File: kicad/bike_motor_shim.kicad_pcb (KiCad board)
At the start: 2 copper layers, 26.7 x 19 mm, 13 parts, among them J1 Conn_01x06_Male, J2 Conn_01x06_Male, K1 MSxx-1Axx-75, U1 ATtiny45-20SU, U2 MCP1700-5002E_SOT23, Y1 Crystal_Small

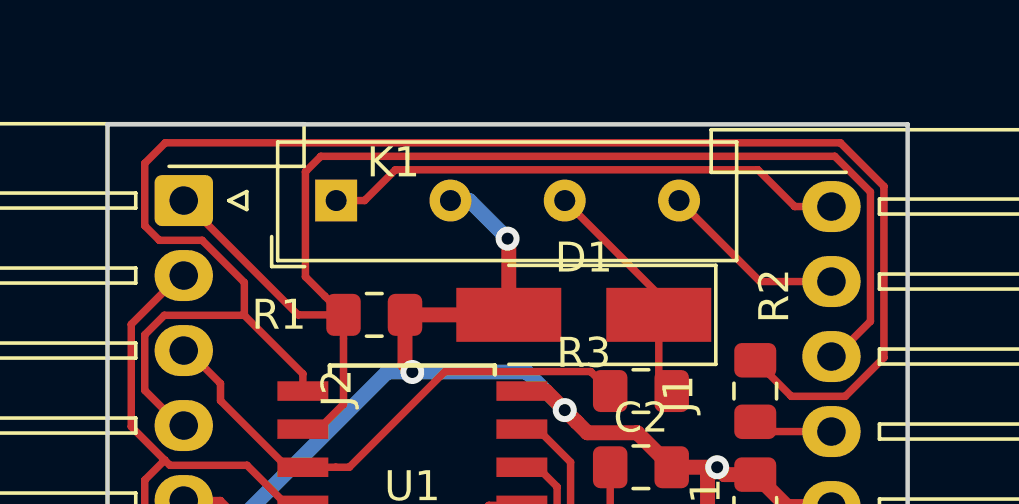
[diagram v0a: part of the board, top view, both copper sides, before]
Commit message: Fixed relay footprint
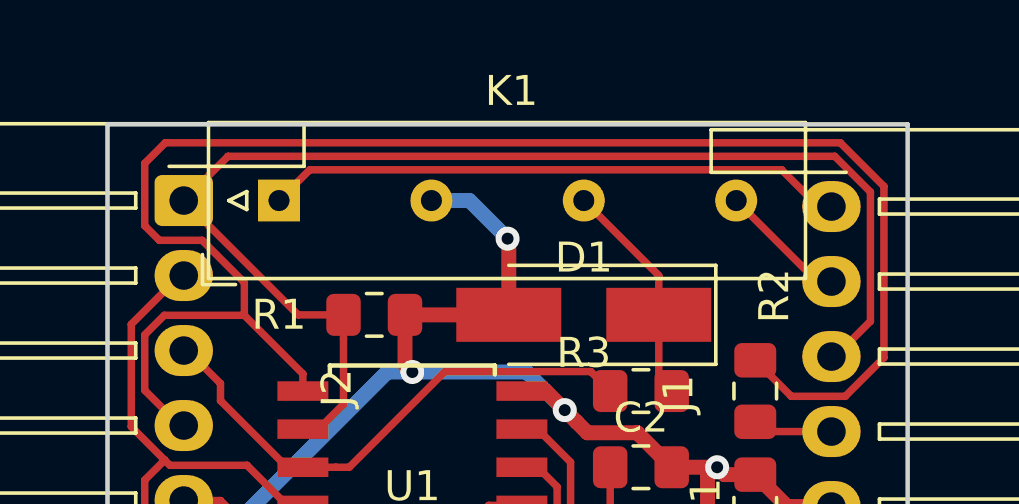
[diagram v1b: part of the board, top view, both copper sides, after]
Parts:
- K1: footprint Relay_THT:Relay_SPST_StandexMeder_MS_Form1AB -> Relay_THT:Relay_SPST_StandexMeder_SIL_Form1A
- moved K1 1.91 mm to (142.9, 112.4)
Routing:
- net MOTOR_OUT: track 6.20 -> 4.29 mm
- net MOTOR_IN: track 17.4 -> 19.3 mm
- net MISO: track 42.5 -> 41.7 mm
- net GND: track 40.7 -> 41.3 mm

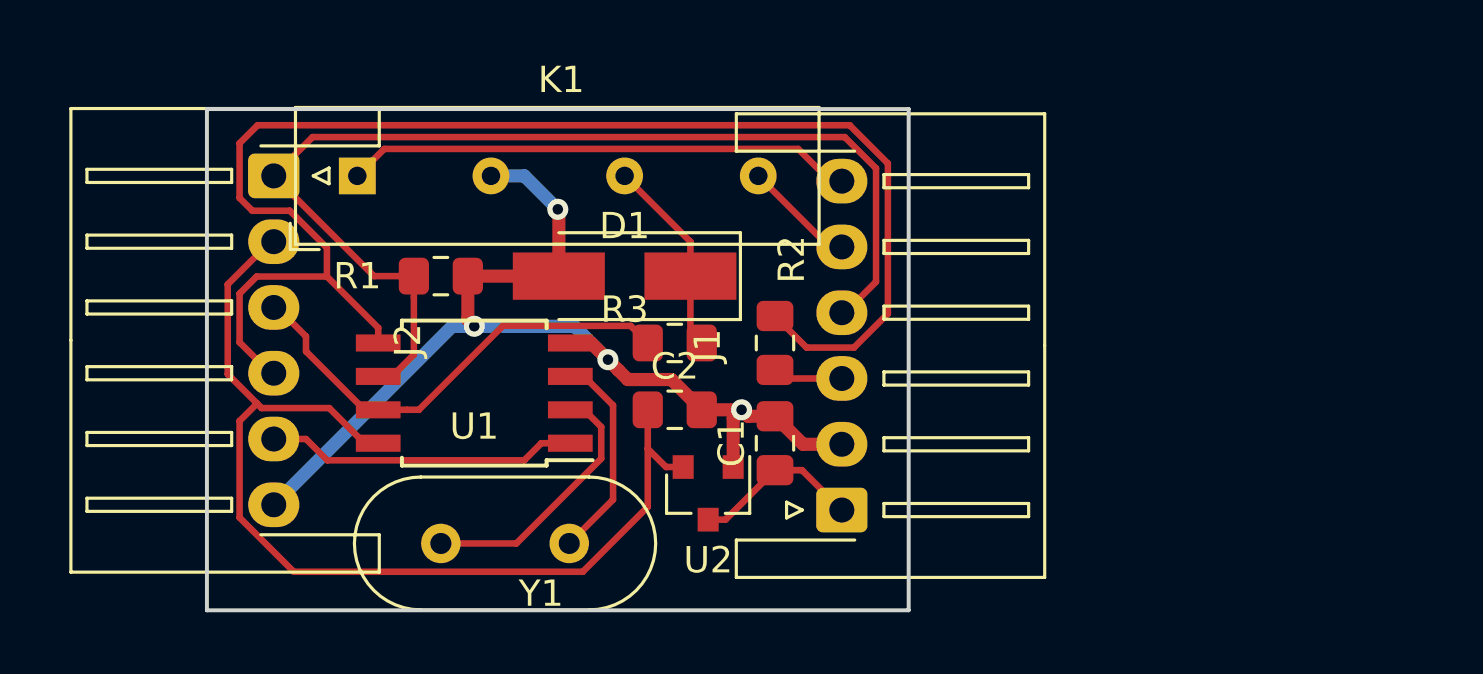
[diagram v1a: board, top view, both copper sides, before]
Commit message: Adding bypass relay and LEDs.
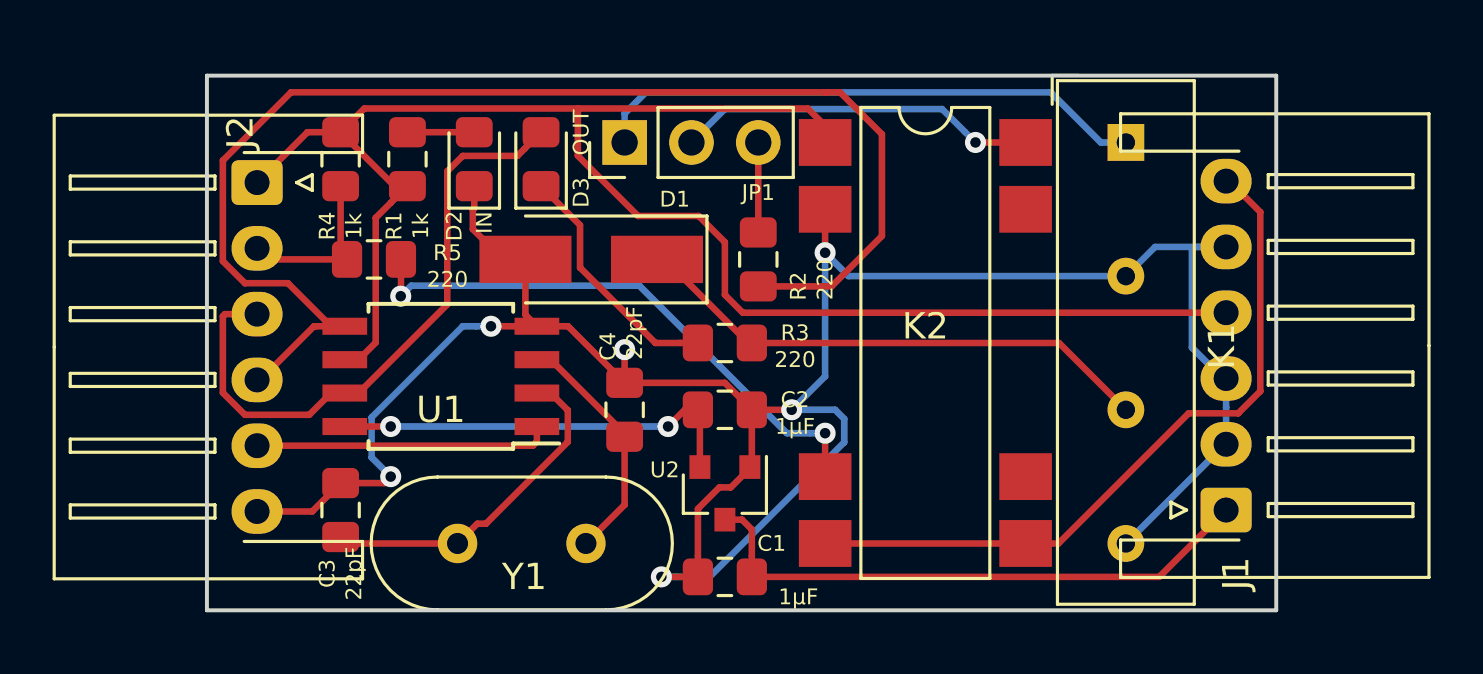
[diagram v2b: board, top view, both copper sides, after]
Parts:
- added C3: 22pF, Capacitor_SMD:C_0805_2012Metric_Pad1.15x1.40mm_HandSolder, F.Cu at (142.2, 125.1)
- added C4: 22pF, Capacitor_SMD:C_0805_2012Metric_Pad1.15x1.40mm_HandSolder, F.Cu at (153.0, 121.3)
- added D2: IN, LED_SMD:LED_0805_2012Metric_Pad1.15x1.40mm_HandSolder, F.Cu at (147.3, 111.8)
- added D3: OUT, LED_SMD:LED_0805_2012Metric_Pad1.15x1.40mm_HandSolder, F.Cu at (149.9, 111.8)
- added JP1: Jumper_NC_Dual, Connector_PinHeader_2.54mm:PinHeader_1x03_P2.54mm_Vertical, F.Cu at (153.0, 111.1)
- added K2: DIPxx-1Cxx-51x, trr-relay:TRR-RELAY-SMDIP-14_W7.62mm, F.Cu at (164.5, 118.7)
- added R4: 1k, Resistor_SMD:R_0805_2012Metric_Pad1.15x1.40mm_HandSolder, F.Cu at (142.2, 111.8)
- added R5: 220, Resistor_SMD:R_0805_2012Metric_Pad1.15x1.40mm_HandSolder, F.Cu at (143.5, 115.6)
- moved K1 29.2 mm to (172.1, 111.1), turned to 270 degrees
- moved J1 14.6 mm to (175.9, 125.1)
- moved G*** 6.98 mm to (157.5, 119.4)
- moved C1 5.43 mm to (156.8, 127.6), turned to 180 degrees
- moved R1 4.62 mm to (144.8, 111.8), turned to 90 degrees
- moved R2 3.24 mm to (158.1, 115.6), turned to 270 degrees
- moved C2 1.91 mm to (156.8, 121.3)
- moved R3 1.91 mm to (156.8, 118.7)
- moved D1 1.42 mm to (151.8, 115.6)
- moved U1 1.42 mm to (146.1, 120.0)
- moved J2 0.68 mm to (139.1, 112.6)
- moved U2 0.63 mm to (156.8, 124.5)
- moved Y1 0.63 mm to (146.7, 126.4)
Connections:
- C1 pad 2: GND -> MOTOR_OUT
- C2 pad 2: GND -> MOTOR_OUT
- D1 pad 2: GND -> MOTOR_OUT
- J1 pad 2: GND -> MOTOR_OUT
- J1 pad 3: SENSOR_OUT -> MOTOR_OUT
- J2 pad 6: GND -> MOTOR_OUT
- K1 pad 1: MOTOR_IN -> MOTOR_DRY
- K1 pad 3: GND -> MOTOR_OUT
- R1 pad 2: GND -> Net-(D2-Pad2)
- R2 pad 1: SENSOR_OUT -> MOTOR_TTL
- R3 pad 1: SCK -> Net-(D3-Pad1)
- U1 pad 4: GND -> MOTOR_OUT
- U2 pad 1: GND -> MOTOR_OUT
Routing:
- net MOTOR_OUT: track 4.29 -> 94.9 mm, vias 0 -> 6
- net GND: track 41.3 -> 0.00 mm, vias 4 -> 0
- net MISO: track 41.7 -> 65.0 mm
- net Net-(K2-Pad6): track 0.00 -> 21.7 mm, vias 0 -> 2
- net MOTOR_DRY: track 0.00 -> 21.3 mm
- net +5V: track 40.0 -> 22.8 mm, vias 0 -> 2
- net +6V: track 6.49 -> 22.2 mm
- net Net-(JP1-Pad2): track 0.00 -> 13.8 mm, vias 0 -> 1
- net Net-(D1-Pad1): track 8.24 -> 20.2 mm
- net Net-(D3-Pad1): track 0.00 -> 9.37 mm
- net MOTOR_IN: track 19.3 -> 27.5 mm
- net SCK: track 17.9 -> 24.1 mm
- net MOSI: track 54.4 -> 49.9 mm
- net Net-(C3-Pad2): track 10.1 -> 13.5 mm
- net MOTOR_TTL: track 0.00 -> 3.42 mm
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- added copper zone on B.Cu, net MOTOR_OUT
- removed copper zone on B.Cu, net GND
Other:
- board size 26.7 x 19 mm -> 40.6 x 20.3 mm
- board text added: "DRY"
- board text added: "MOSI"
- board text added: "MOTOR"
- board text added: "RST"
- board text added: "SCK"
- board text added: "SENSOR"
- board text added: "TTL"
- board text removed: "motor"

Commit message: Fixing traces.
Adding missed trace and increasing width of ground and power traces.
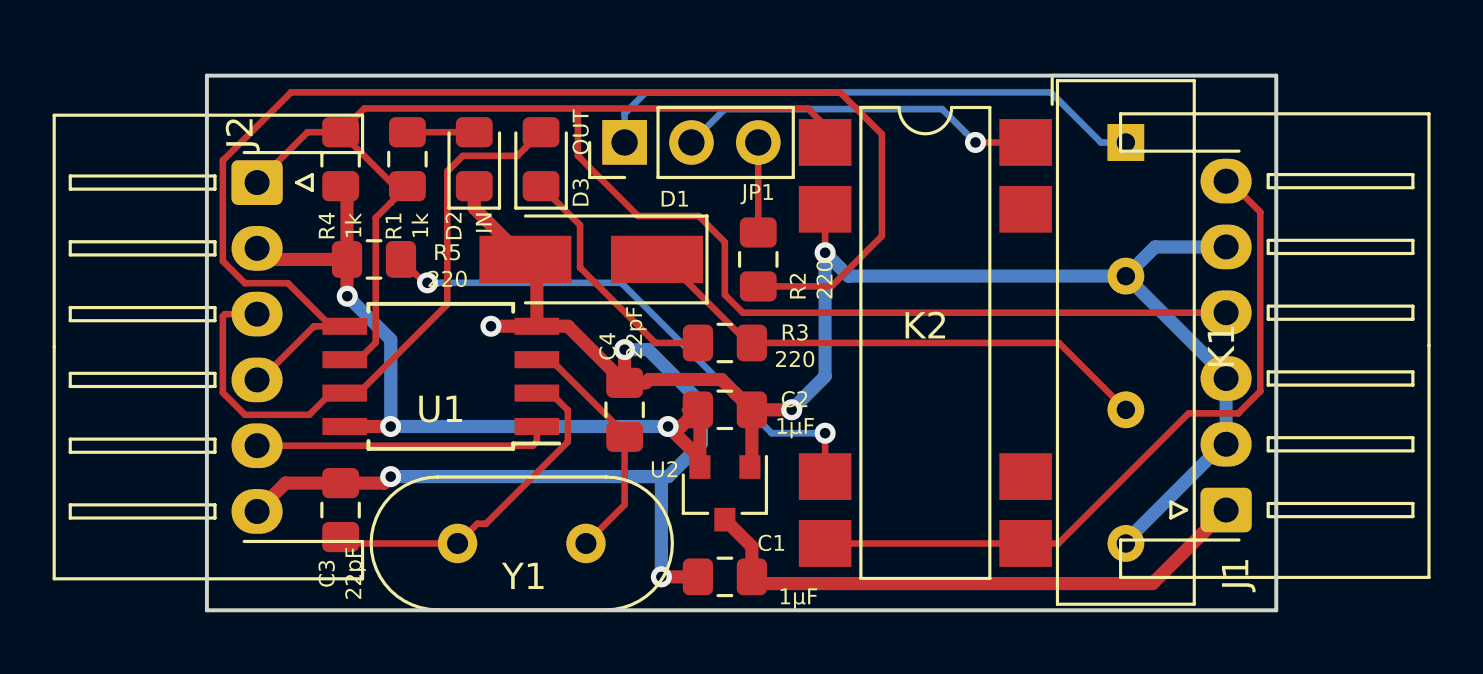
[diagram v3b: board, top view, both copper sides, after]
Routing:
- net +5V: track 22.8 -> 32.7 mm, vias 2 -> 3
- net MOTOR_OUT: track 94.9 -> 90.1 mm
- net Net-(K2-Pad6): track 21.7 -> 20.5 mm
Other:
- net class +5V added: clearance 0.2, trace_width 0.5, via_dia 0.8, via_drill 0.4
- board text added: "2019.07.25"
- board text added: "https://github.com/mar0x/bike_motor_shim"

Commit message: Board and sketch improvements.
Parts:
- removed R5: 220, Resistor_SMD:R_0805_2012Metric_Pad1.15x1.40mm_HandSolder
- added Q1: S8050, Package_TO_SOT_SMD:SOT-23, F.Cu at (163.3, 115.6)
- D1: footprint Diode_SMD:D_SMA_Handsoldering -> Diode_SMD:D_SMA
- K2: value DIPxx-1Cxx-51x -> G6K-2; footprint trr-relay:TRR-RELAY-SMDIP-14_W7.62mm -> Relay_SMD:Relay_DPDT_Omron_G6K-2F-Y
- moved D1 15.4 mm to (167.1, 114.0), turned to 270 degrees
- moved K1 15.2 mm to (172.1, 126.4), turned to 90 degrees
- moved JP1 5.34 mm to (158.4, 110.9), turned to 270 degrees
- moved R2 5.00 mm to (153.5, 113.5), turned to 180 degrees
- moved K2 4.70 mm to (164.5, 123.4), turned to 180 degrees
- moved R3 3.99 mm to (159.3, 115.6), turned to 180 degrees
- moved G*** 0.89 mm to (157.5, 118.5)
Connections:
- C1 pad 2: MOTOR_OUT -> GND
- C2 pad 2: MOTOR_OUT -> GND
- C3 pad 1: MOTOR_OUT -> GND
- C4 pad 1: MOTOR_OUT -> GND
- D1 pad 1: Net-(D1-Pad1) -> +5V
- D1 pad 2: MOTOR_OUT -> Net-(D1-Pad2)
- D2 pad 1: MOTOR_OUT -> GND
- J1 pad 2: MOTOR_OUT -> GND
- J1 pad 3: MOTOR_OUT -> GND
- J1 pad 4: MISO -> SENSOR_IN
- J1 pad 5: MOTOR_OUT -> GND
- J2 pad 6: MOTOR_OUT -> GND
- K1 pad 1: MOTOR_DRY -> GND
- K1 pad 3: MOTOR_OUT -> Net-(D1-Pad2)
- K1 pad 5: Net-(D1-Pad1) -> +5V
- K1 pad 7: MOTOR_OUT -> MOTOR_DRY
- K2 pad 1: MISO -> +5V
- K2 pad 2: MOTOR_OUT -> SENSOR_IN
- K2 pad 6: Net-(K2-Pad6) -> SENSOR_IN
- K2 pad 8: MOTOR_IN -> GND
- R3 pad 1: Net-(D3-Pad1) -> Net-(Q1-Pad1)
- R3 pad 2: Net-(D1-Pad1) -> Net-(D3-Pad1)
- U1 pad 4: MOTOR_OUT -> GND
- U2 pad 1: MOTOR_OUT -> GND
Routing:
- net GND: track 0.00 -> 95.1 mm, vias 0 -> 6
- net MOTOR_OUT: track 90.1 -> 0.00 mm, vias 6 -> 0
- net +5V: track 32.7 -> 73.4 mm, vias 3 -> 6
- net MISO: track 65.0 -> 34.6 mm, vias 0 -> 2
- net SENSOR_IN: track 0.00 -> 24.6 mm
- net Net-(K2-Pad6): track 20.5 -> 0.00 mm, vias 2 -> 0
- net Net-(D1-Pad1): track 20.2 -> 0.00 mm
- net MOSI: track 49.9 -> 31.9 mm
- net Net-(D1-Pad2): track 0.00 -> 12.5 mm
- net MOTOR_DRY: track 21.3 -> 14.5 mm
- net MOTOR_IN: track 27.5 -> 24.2 mm
- net Net-(JP1-Pad2): track 13.8 -> 16.8 mm, vias 1 -> 0
- net Net-(Q1-Pad1): track 0.00 -> 2.50 mm
- added copper zone on B.Cu, net GND
- removed copper zone on B.Cu, net MOTOR_OUT
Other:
- board text added: "2019.07.30"
- board text removed: "2019.07.25"
